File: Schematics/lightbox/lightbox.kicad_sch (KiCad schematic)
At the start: 36 parts, among them J1 Screw_Terminal_01x04, J2 Conn_01x11_Female, J3 Conn_01x07_Female, J4 Conn_02x03_Odd_Even, Q1 IRF530, Q2 IRF530, SW1 SW_Push_-, SW2 SW_Push_Reset, SW3 SW_Push_+, SW4 SW_Push_START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

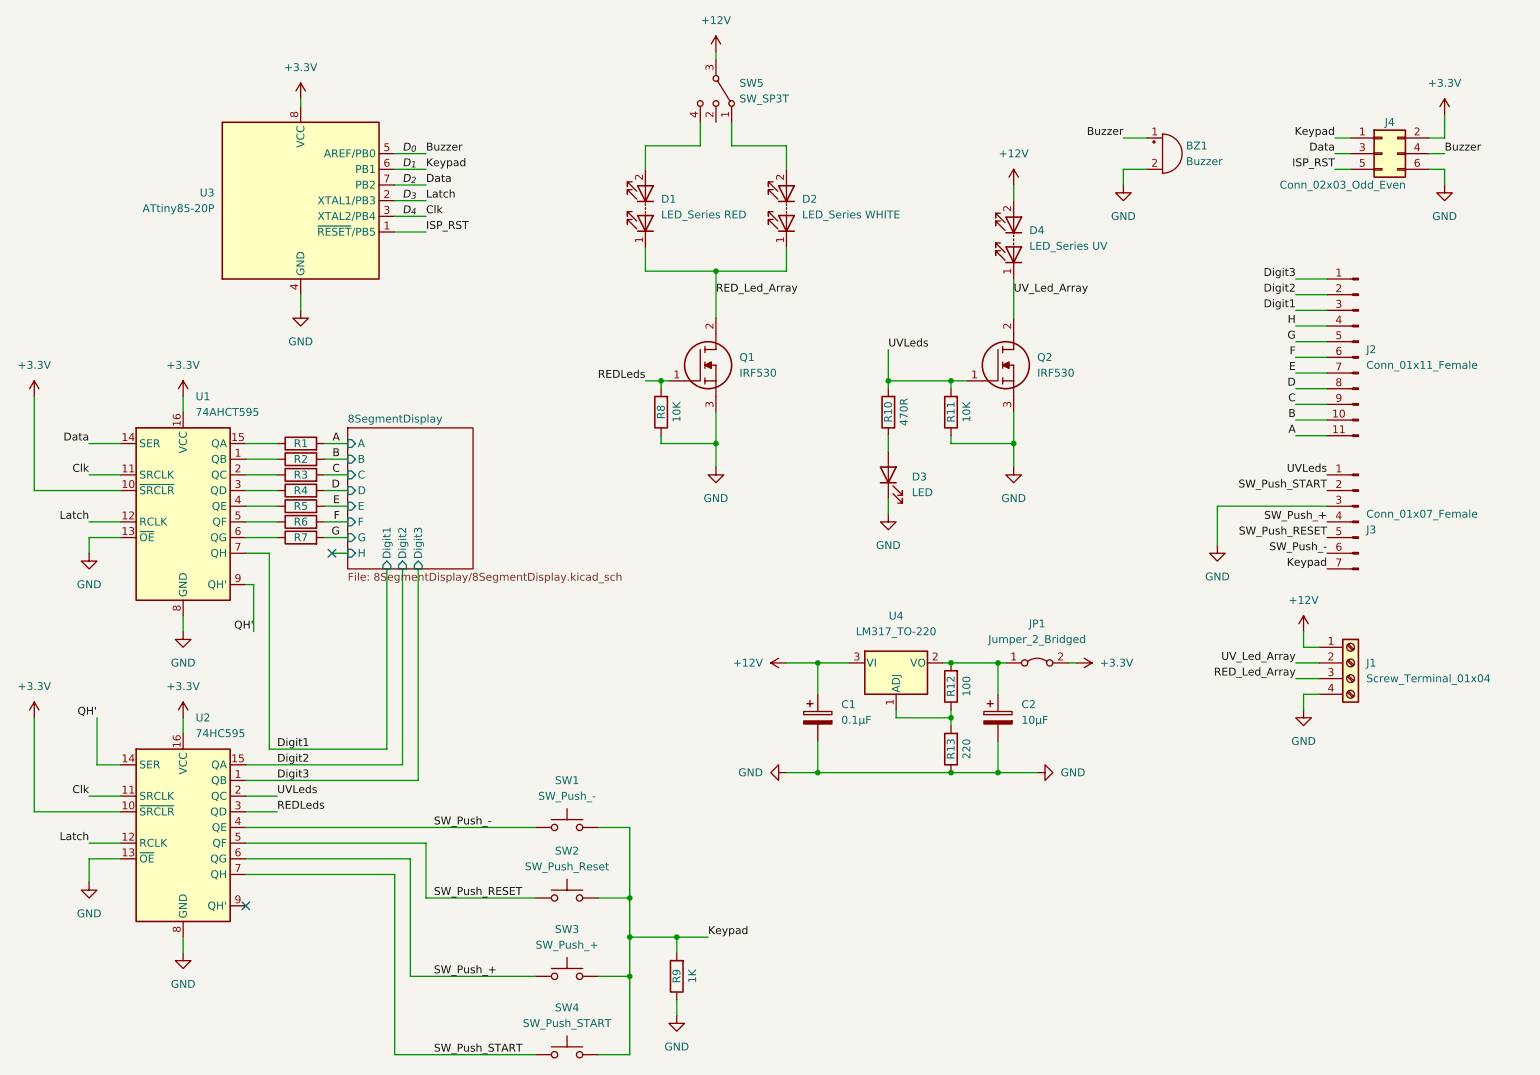
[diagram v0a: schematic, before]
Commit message: Update lightbox design
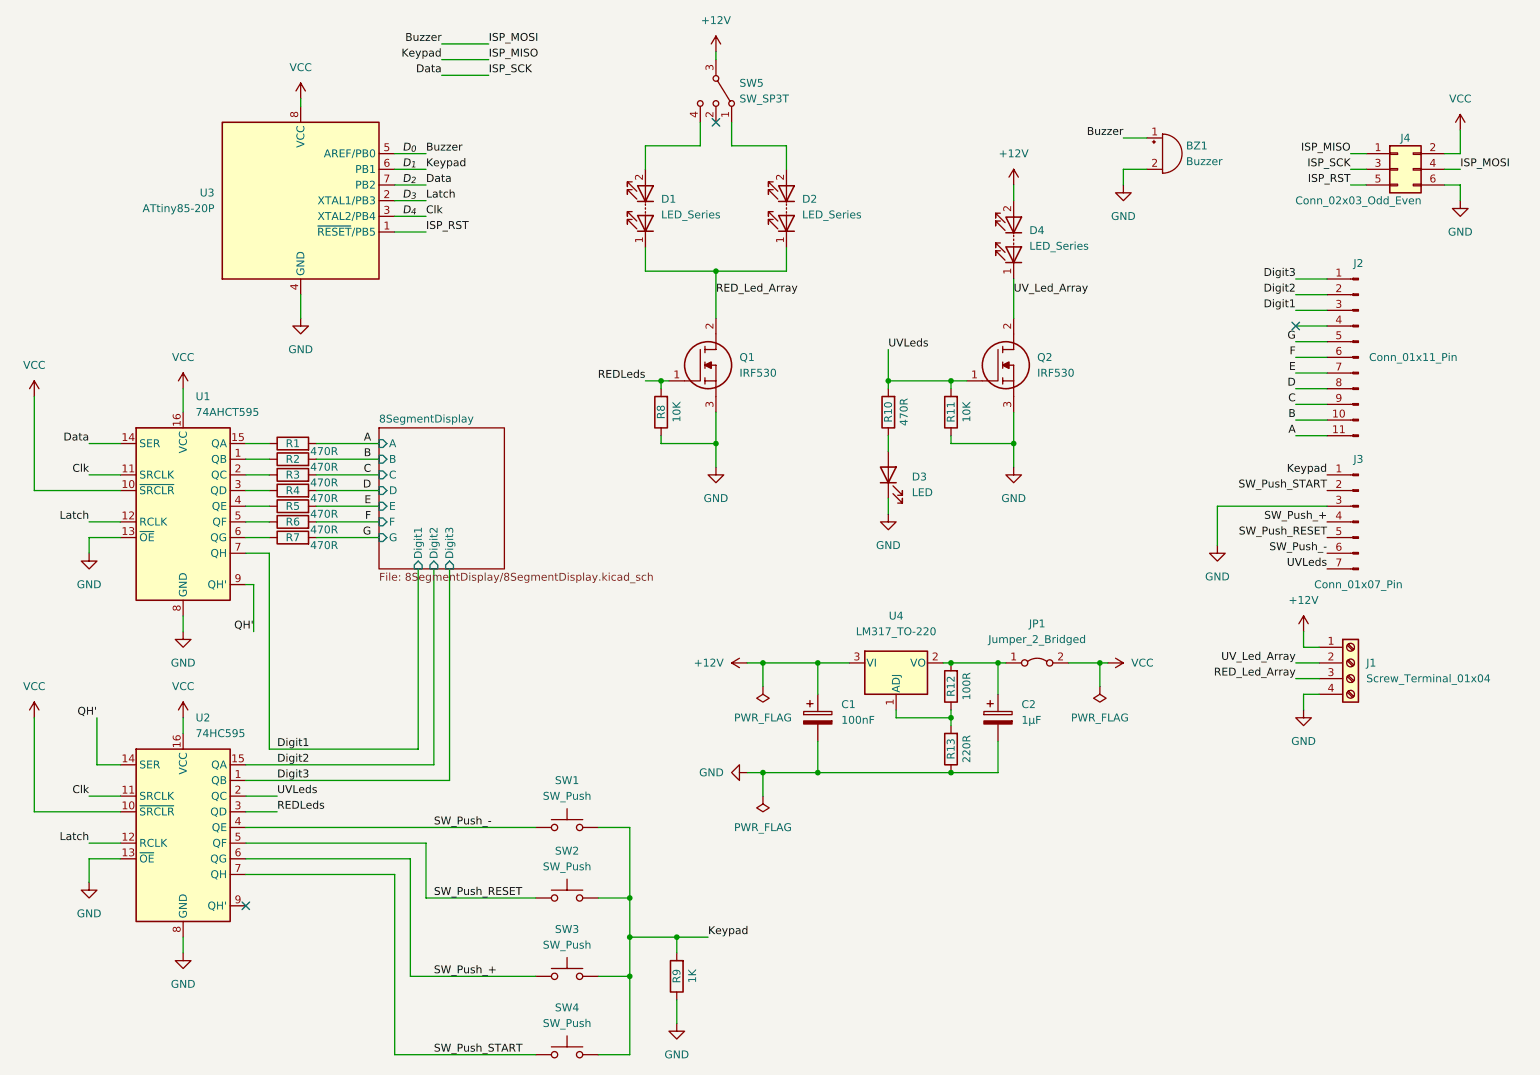
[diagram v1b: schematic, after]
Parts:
- C1: value 0.1µF -> 100nF; footprint Capacitor_THT:CP_Radial_D4.0mm_P1.50mm -> Capacitor_THT:CP_Radial_D6.3mm_P2.50mm
- C2: value 10µF -> 1µF; footprint Capacitor_THT:CP_Radial_D4.0mm_P1.50mm -> Capacitor_THT:CP_Radial_D6.3mm_P2.50mm
- D1: value LED_Series RED -> LED_Series
- D2: value LED_Series WHITE -> LED_Series
- D4: value LED_Series UV -> LED_Series
- J2: value Conn_01x11_Female -> Conn_01x11_Pin; footprint Connector_PinHeader_1.27mm:PinHeader_1x12_P1.27mm_Horizontal -> Connector_PinHeader_2.54mm:PinHeader_1x12_P2.54mm_Horizontal; symbol Connector:Conn_01x11_Male -> Connector:Conn_01x11_Pin
- J3: value Conn_01x07_Female -> Conn_01x07_Pin; footprint Connector_PinHeader_1.27mm:PinHeader_1x07_P1.27mm_Horizontal -> Connector_PinHeader_2.54mm:PinHeader_1x07_P2.54mm_Horizontal; symbol Connector:Conn_01x07_Male -> Connector:Conn_01x07_Pin
- J4: footprint Connector_PinHeader_1.27mm:PinHeader_2x03_P1.27mm_Vertical -> Connector_PinHeader_2.54mm:PinHeader_2x03_P2.54mm_Vertical
- JP1: footprint Connector_PinHeader_1.27mm:PinHeader_1x02_P1.27mm_Vertical -> Connector_PinHeader_2.54mm:PinHeader_1x02_P2.54mm_Vertical
- Q1, Q2: footprint Package_TO_SOT_THT:TO-220-3_Vertical -> TO255P460X1020X2008-3P
- R1, R10, R11, R2, R3, R4, R5, R6, R7, R8, R9: footprint Resistor_THT:R_Axial_DIN0204_L3.6mm_D1.6mm_P5.08mm_Vertical -> Resistor_THT:R_Axial_DIN0204_L3.6mm_D1.6mm_P5.08mm_Horizontal
- R12: value 100 -> 100R; footprint Resistor_THT:R_Axial_DIN0204_L3.6mm_D1.6mm_P5.08mm_Vertical -> Resistor_THT:R_Axial_DIN0204_L3.6mm_D1.6mm_P5.08mm_Horizontal
- R13: value 220 -> 220R; footprint Resistor_THT:R_Axial_DIN0204_L3.6mm_D1.6mm_P5.08mm_Vertical -> Resistor_THT:R_Axial_DIN0204_L3.6mm_D1.6mm_P5.08mm_Horizontal
- SW1: value SW_Push_- -> SW_Push
- SW2: value SW_Push_Reset -> SW_Push
- SW3: value SW_Push_+ -> SW_Push
- SW4: value SW_Push_START -> SW_Push
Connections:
- net D_{1}: now also J3.1 (Pin_1); no longer J3.7 (Pin_7)
- net UVLeds: now also J3.7 (Pin_7); no longer J3.1 (Pin_1)
- net +3V3 renamed VCC
- net H: no longer names the net of J2.4 (Pin_4)
- no-connect marks 2 -> 3
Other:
- sheet 8SegmentDisplay ports: added none; removed H
- moved on the sheet: J4, R1, R2, R3, R4, R5, R6, R7
